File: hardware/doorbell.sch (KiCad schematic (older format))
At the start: 16 parts, among them J1 CONN_01X02, J2 CONN_01X09, J3 CONN_01X07, P1 DOOR, P2 STRIP_CONN, Q1 MMBT3904, U1 LD1117S33CTR, U2 4N25, U3 ESP-12

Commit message: Fix some library issues
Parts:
- removed P1: DOOR, Terminal_Blocks:TerminalBlock_Pheonix_MPT-2.54mm_3pol, symbol DOOR
- added P1: DOOR_CONN, Terminal_Blocks:TerminalBlock_Pheonix_MPT-2.54mm_3pol, symbol DOOR_CONN
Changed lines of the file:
@@
 EESchema Schematic File Version 2
-LIBS:borniers
 LIBS:power
 LIBS:device
@@
 Text GLabel 2100 1150 0    60   Input ~ 0
 VIN
-$Comp
-L DOOR P1
-U 1 1 573DA8E3
-P 1200 2050
-F 0 "P1" H 1100 2300 50  0000 C CNN
-F 1 "DOOR" H 1200 2240 40  0000 C CNN
-F 2 "Terminal_Blocks:TerminalBlock_Pheonix_MPT-2.54mm_3pol" H 1200 2050 60  0001 C CNN
-F 3 "" H 1200 2050 60  0000 C CNN
-	1    1200 2050
-	-1   0    0    1
-$EndComp
 Text GLabel 1550 2150 2    60   Input ~ 0
 VIN
@@
 	-1   0    0    1
 $EndComp
+$Comp
+L DOOR_CONN P1
+U 1 1 5744979E
+P 1350 2050
+F 0 "P1" H 1350 2250 50  0000 C CNN
+F 1 "DOOR_CONN" V 1450 2050 50  0000 C CNN
+F 2 "Terminal_Blocks:TerminalBlock_Pheonix_MPT-2.54mm_3pol" H 1350 2050 50  0001 C CNN
+F 3 "" H 1350 2050 50  0000 C CNN
+	1    1350 2050
+	-1   0    0    1
+$EndComp

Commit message: Shrink board, expand copper, change Q1 bom
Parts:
- removed Q1: MMBT3904, TO_SOT_Packages_SMD:SOT-23, symbol MMBT3904
- added Q1: BC_846B, TO_SOT_Packages_SMD:SOT-23_Handsoldering, symbol Q_NPN_BEC
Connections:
- net GND: now also Q1.2 (E)
- net at U2.2: now also Q1.3 (C)
- net at R6.2: now also Q1.1 (B)
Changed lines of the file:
@@
-$EndComp
-$Comp
-L MMBT3904 Q1
-U 1 1 574330E7
-P 4350 4650
-F 0 "Q1" H 4550 4725 50  0000 L CNN
-F 1 "MMBT3904" H 4550 4650 50  0000 L CNN
-F 2 "TO_SOT_Packages_SMD:SOT-23" H 4550 4575 50  0000 L CIN
-F 3 "" H 4350 4650 50  0000 L CNN
-	1    4350 4650
-	-1   0    0    1
 $EndComp
 $Comp
@@
 	-1   0    0    1
 $EndComp
+$Comp
+L Q_NPN_BEC Q1
+U 1 1 5745933D
+P 4350 4650
+F 0 "Q1" H 4650 4700 50  0000 R CNN
+F 1 "BC_846B" H 4950 4600 50  0000 R CNN
+F 2 "TO_SOT_Packages_SMD:SOT-23_Handsoldering" H 4550 4750 50  0001 C CNN
+F 3 "" H 4350 4650 50  0000 C CNN
+	1    4350 4650
+	-1   0    0    1
+$EndComp

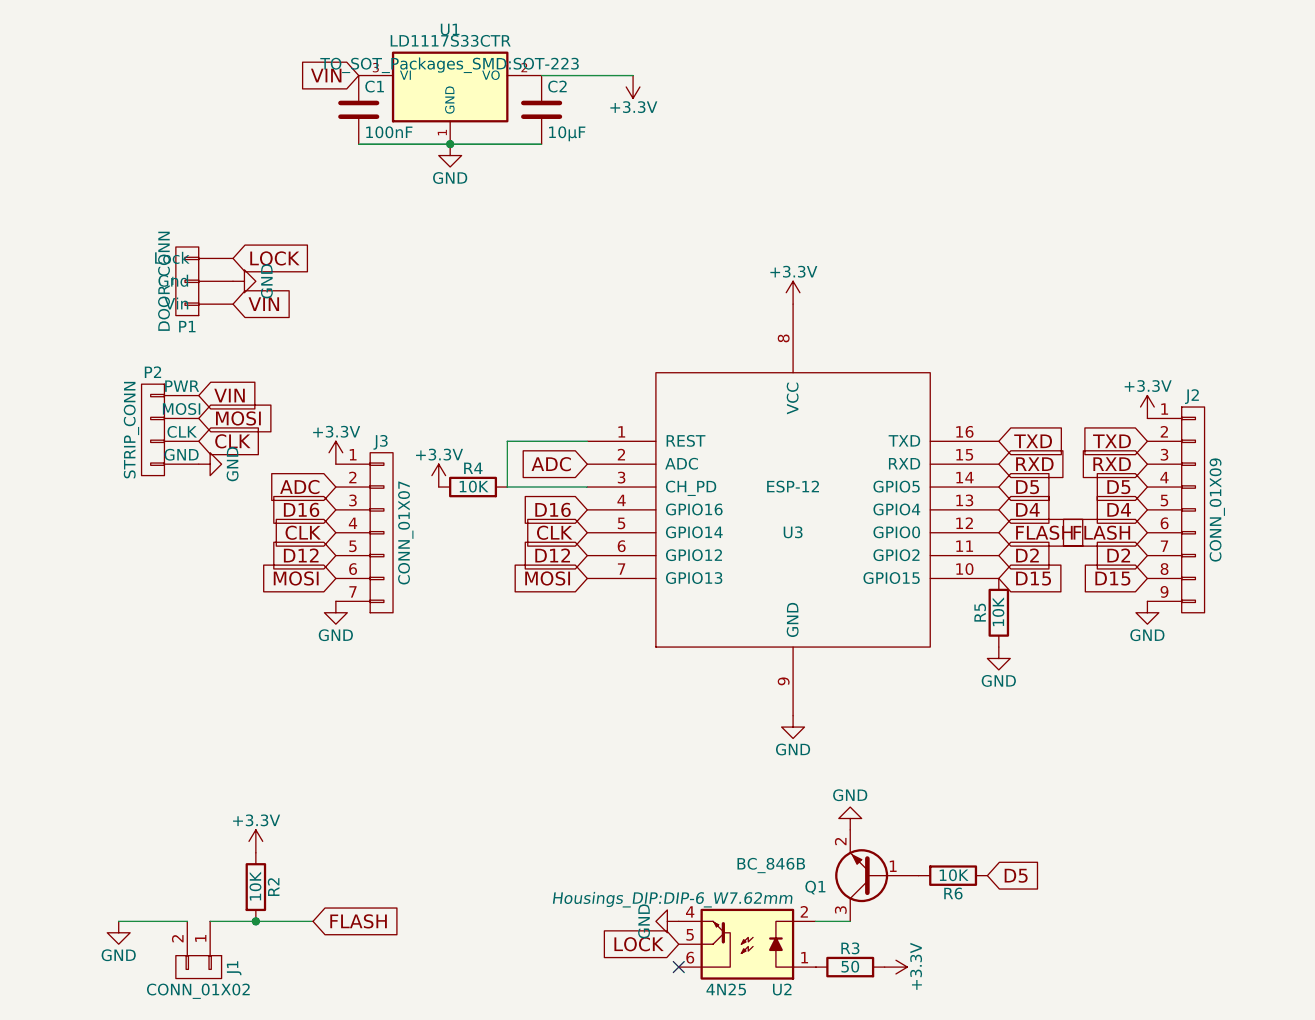
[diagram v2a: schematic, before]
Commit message: Convert to include a switching voltage regulator breakout
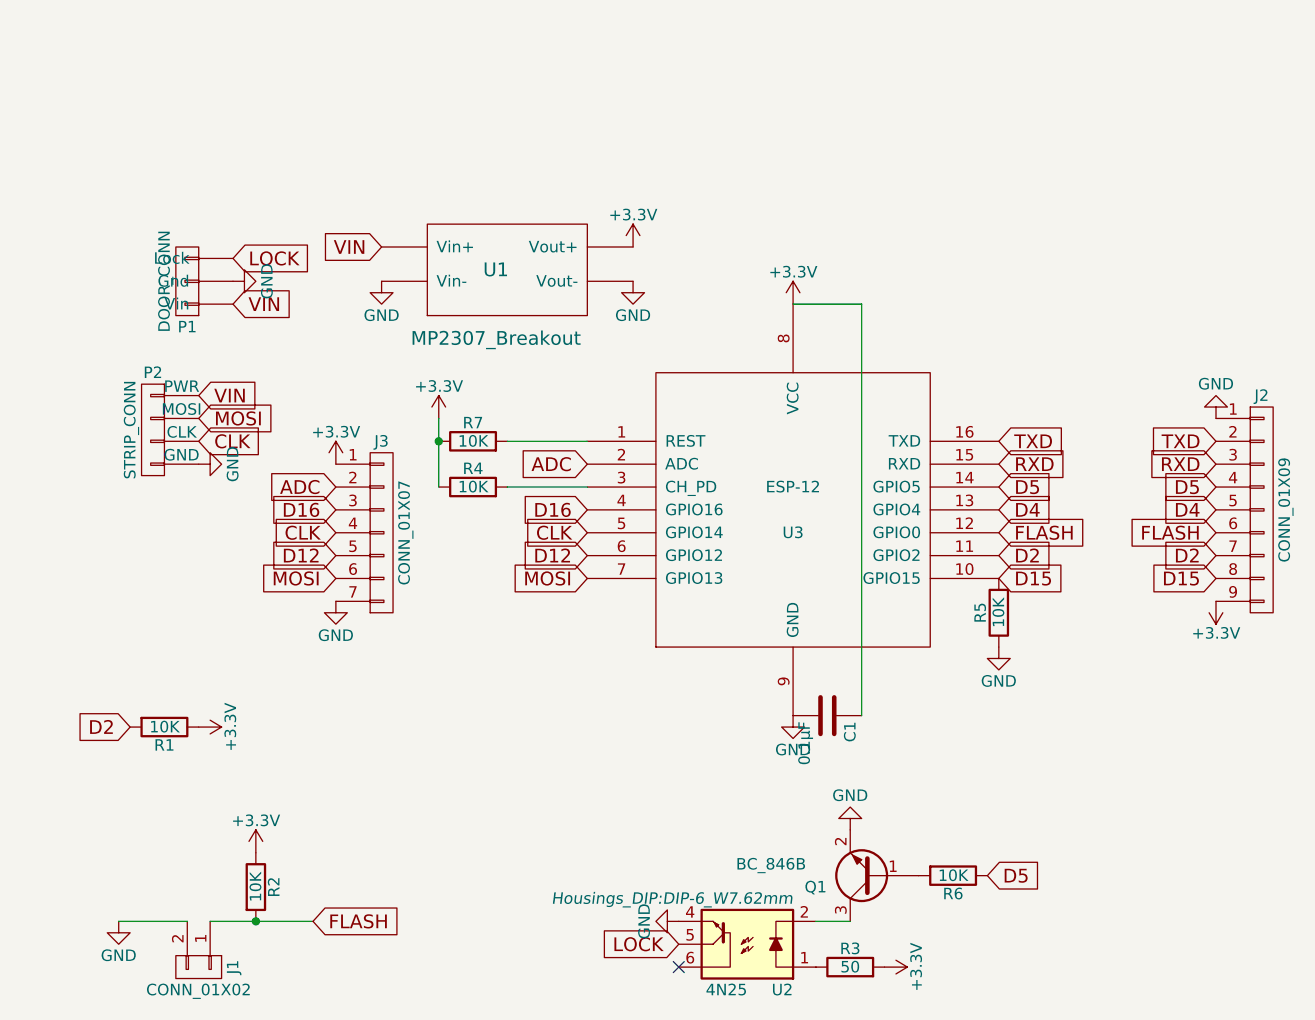
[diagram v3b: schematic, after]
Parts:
- removed C2: 10µF, Capacitors_SMD:C_0805_HandSoldering, symbol C
- removed U1: LD1117S33CTR, TO_SOT_Packages_SMD:SOT-223, symbol LD1117S33CTR
- added R1, R7: 10K, symbol R
- added U1: MP2307_Breakout, Doorbell:MP2307_Breakout, symbol MP2307_Breakout
- C1: value 100nF -> 0.1µF; footprint Capacitors_SMD:C_0805_HandSoldering -> Capacitors_SMD:C_1206_HandSoldering
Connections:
- net +3V3: now also C1.1, J2.9 (P9), R1.1, R7.1, U1.3 (Vout+); no longer J2.1 (P1)
- net D2: now also R1.2
- net GND: now also J2.1 (P1), U1.2 (Vin-), U1.4 (Vout-); no longer J2.9 (P9)
- net VIN: now also U1.1 (Vin+); no longer C1.1
- net at R4.2, U3.3 (CH_PD): no longer U3.1 (REST)
- new net: R7.2, U3.1 (REST)
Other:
- moved on the sheet: J2

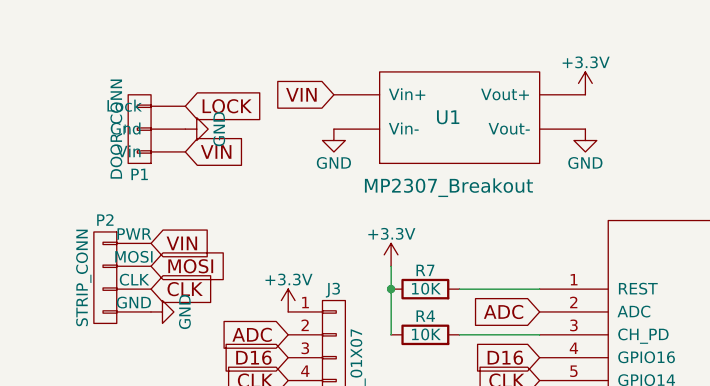
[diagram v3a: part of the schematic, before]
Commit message: Add Vin decoupling cap
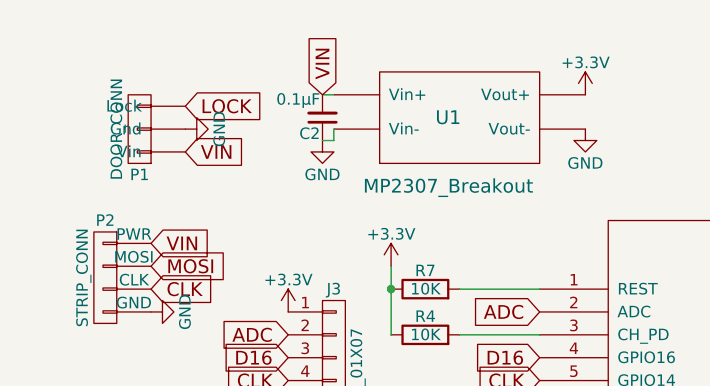
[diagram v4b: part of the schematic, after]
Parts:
- added C2: 0.1µF, Capacitors_SMD:C_1206_HandSoldering, symbol C_Small
- R1, R7: footprint (none) -> Resistors_ThroughHole:Resistor_Vertical_RM5mm
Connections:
- net GND: now also C2.1
- net VIN: now also C2.2
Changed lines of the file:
@@
 MOSI
 $Comp
-L GND #PWR14
+L GND #PWR01
 U 1 1 573B5931
 P 4000 3950
-F 0 "#PWR14" H 4000 3700 50  0001 C CNN
+F 0 "#PWR01" H 4000 3700 50  0001 C CNN
 F 1 "GND" H 4000 3800 50  0000 C CNN
 F 2 "" H 4000 3950 50  0000 C CNN
@@
 $EndComp
 $Comp
-L +3.3V #PWR13
+L +3.3V #PWR02
 U 1 1 573B599B
 P 4000 2150
-F 0 "#PWR13" H 4000 2000 50  0001 C CNN
+F 0 "#PWR02" H 4000 2000 50  0001 C CNN
 F 1 "+3.3V" H 4000 2290 50  0000 C CNN
 F 2 "" H 4000 2150 50  0000 C CNN
@@
 $EndComp
 $Comp
-L GND #PWR17
+L GND #PWR03
 U 1 1 573C748A
 P 4900 3650
-F 0 "#PWR17" H 4900 3400 50  0001 C CNN
+F 0 "#PWR03" H 4900 3400 50  0001 C CNN
 F 1 "GND" H 4900 3500 50  0000 C CNN
 F 2 "" H 4900 3650 50  0000 C CNN
@@
 	3100 2950 2750 2950
 $Comp
-L +3.3V #PWR9
+L +3.3V #PWR04
 U 1 1 573C76A9
 P 2450 2650
-F 0 "#PWR9" H 2450 2500 50  0001 C CNN
+F 0 "#PWR04" H 2450 2500 50  0001 C CNN
 F 1 "+3.3V" H 2450 2790 50  0000 C CNN
 F 2 "" H 2450 2650 50  0000 C CNN
@@
 $EndComp
 $Comp
-L GND #PWR1
+L GND #PWR05
 U 1 1 573C7B17
 P 1050 4850
-F 0 "#PWR1" H 1050 4600 50  0001 C CNN
+F 0 "#PWR05" H 1050 4600 50  0001 C CNN
 F 1 "GND" H 1050 4700 50  0000 C CNN
 F 2 "" H 1050 4850 50  0000 C CNN
@@
 $EndComp
 $Comp
-L +3.3V #PWR5
+L +3.3V #PWR06
 U 1 1 573C7B23
 P 1650 4550
-F 0 "#PWR5" H 1650 4400 50  0001 C CNN
+F 0 "#PWR06" H 1650 4400 50  0001 C CNN
 F 1 "+3.3V" H 1650 4690 50  0000 C CNN
 F 2 "" H 1650 4550 50  0000 C CNN
@@
 LOCK
 $Comp
-L GND #PWR12
+L GND #PWR07
 U 1 1 573C8ED6
 P 3500 4850
-F 0 "#PWR12" H 3500 4600 50  0001 C CNN
+F 0 "#PWR07" H 3500 4600 50  0001 C CNN
 F 1 "GND" H 3500 4700 50  0000 C CNN
 F 2 "" H 3500 4850 50  0000 C CNN
@@
 $EndComp
 $Comp
-L +3.3V #PWR16
+L +3.3V #PWR08
 U 1 1 573C96C2
 P 4400 5050
-F 0 "#PWR16" H 4400 4900 50  0001 C CNN
+F 0 "#PWR08" H 4400 4900 50  0001 C CNN
 F 1 "+3.3V" H 4400 5190 50  0000 C CNN
 F 2 "" H 4400 5050 50  0000 C CNN
@@
 	4100 4850 4250 4850
 $Comp
-L GND #PWR15
+L GND #PWR09
 U 1 1 573C9852
 P 4250 4450
-F 0 "#PWR15" H 4250 4200 50  0001 C CNN
+F 0 "#PWR09" H 4250 4200 50  0001 C CNN
 F 1 "GND" H 4250 4300 50  0000 C CNN
 F 2 "" H 4250 4450 50  0000 C CNN
@@
 LOCK
 $Comp
-L GND #PWR4
+L GND #PWR010
 U 1 1 573DAD82
 P 1550 2050
-F 0 "#PWR4" H 1550 1800 50  0001 C CNN
+F 0 "#PWR010" H 1550 1800 50  0001 C CNN
 F 1 "GND" H 1550 1900 50  0000 C CNN
 F 2 "" H 1550 2050 50  0000 C CNN
@@
 CLK
 $Comp
-L GND #PWR2
+L GND #PWR011
 U 1 1 573DA44F
 P 1400 2850
-F 0 "#PWR2" H 1400 2600 50  0001 C CNN
+F 0 "#PWR011" H 1400 2600 50  0001 C CNN
 F 1 "GND" H 1400 2700 50  0000 C CNN
 F 2 "" H 1400 2850 50  0000 C CNN
@@
 $EndComp
 $Comp
-L +3.3V #PWR19
+L +3.3V #PWR012
 U 1 1 57430C52
 P 5850 3450
-F 0 "#PWR19" H 5850 3300 50  0001 C CNN
+F 0 "#PWR012" H 5850 3300 50  0001 C CNN
 F 1 "+3.3V" H 5850 3590 50  0000 C CNN
 F 2 "" H 5850 3450 50  0000 C CNN
@@
 D15
 $Comp
-L GND #PWR18
+L GND #PWR013
 U 1 1 57430E1D
 P 5850 2650
-F 0 "#PWR18" H 5850 2400 50  0001 C CNN
+F 0 "#PWR013" H 5850 2400 50  0001 C CNN
 F 1 "GND" H 5850 2500 50  0000 C CNN
 F 2 "" H 5850 2650 50  0000 C CNN
@@
 $EndComp
 $Comp
-L +3.3V #PWR6
+L +3.3V #PWR014
 U 1 1 57431209
 P 2000 2850
-F 0 "#PWR6" H 2000 2700 50  0001 C CNN
+F 0 "#PWR014" H 2000 2700 50  0001 C CNN
 F 1 "+3.3V" H 2000 2990 50  0000 C CNN
 F 2 "" H 2000 2850 50  0000 C CNN
@@
 $EndComp
 $Comp
-L GND #PWR7
+L GND #PWR015
 U 1 1 5743123D
 P 2000 3450
-F 0 "#PWR7" H 2000 3200 50  0001 C CNN
+F 0 "#PWR015" H 2000 3200 50  0001 C CNN
 F 1 "GND" H 2000 3300 50  0000 C CNN
 F 2 "" H 2000 3450 50  0000 C CNN
@@
 	1    0    0    -1
 $EndComp
-Text GLabel 2200 1900 0    60   Input ~ 0
+Text GLabel 2150 1900 1    60   Input ~ 0
 VIN
 $Comp
-L GND #PWR8
+L GND #PWR016
 U 1 1 574C1920
-P 2200 2050
-F 0 "#PWR8" H 2200 1800 50  0001 C CNN
-F 1 "GND" H 2200 1900 50  0000 C CNN
-F 2 "" H 2200 2050 50  0000 C CNN
-F 3 "" H 2200 2050 50  0000 C CNN
-	1    2200 2050
-	1    0    0    -1
-$EndComp
-$Comp
-L GND #PWR11
+P 2150 2100
+F 0 "#PWR016" H 2150 1850 50  0001 C CNN
+F 1 "GND" H 2150 1950 50  0000 C CNN
+F 2 "" H 2150 2100 50  0000 C CNN
+F 3 "" H 2150 2100 50  0000 C CNN
+	1    2150 2100
+	1    0    0    -1
+$EndComp
+$Comp
+L GND #PWR017
 U 1 1 574C19BB
 P 3300 2050
-F 0 "#PWR11" H 3300 1800 50  0001 C CNN
+F 0 "#PWR017" H 3300 1800 50  0001 C CNN
 F 1 "GND" H 3300 1900 50  0000 C CNN
 F 2 "" H 3300 2050 50  0000 C CNN
@@
 $EndComp
 $Comp
-L +3.3V #PWR10
+L +3.3V #PWR018
 U 1 1 574C19ED
 P 3300 1900
-F 0 "#PWR10" H 3300 1750 50  0001 C CNN
+F 0 "#PWR018" H 3300 1750 50  0001 C CNN
 F 1 "+3.3V" H 3300 2040 50  0000 C CNN
 F 2 "" H 3300 1900 50  0000 C CNN
@@
 F 0 "R7" V 2680 2750 50  0000 C CNN
 F 1 "10K" V 2600 2750 50  0000 C CNN
-F 2 "" V 2530 2750 50  0000 C CNN
+F 2 "Resistors_ThroughHole:Resistor_Vertical_RM5mm" V 2530 2750 50  0001 C CNN
 F 3 "" H 2600 2750 50  0000 C CNN
 	1    2600 2750
@@
 F 0 "R1" V 1330 4000 50  0000 C CNN
 F 1 "10K" V 1250 4000 50  0000 C CNN
-F 2 "" V 1180 4000 50  0000 C CNN
+F 2 "Resistors_ThroughHole:Resistor_Vertical_RM5mm" V 1180 4000 50  0001 C CNN
 F 3 "" H 1250 4000 50  0000 C CNN
 	1    1250 4000
@@
 $EndComp
 $Comp
-L +3.3V #PWR3
+L +3.3V #PWR019
 U 1 1 574C2CE0
 P 1400 4000
-F 0 "#PWR3" H 1400 3850 50  0001 C CNN
+F 0 "#PWR019" H 1400 3850 50  0001 C CNN
 F 1 "+3.3V" H 1400 4140 50  0000 C CNN
 F 2 "" H 1400 4000 50  0000 C CNN
@@
 	0    1    1    0
 $EndComp
+$Comp
+L C_Small C2
+U 1 1 574C3EED
+P 2150 2000
+F 0 "C2" H 2160 2070 50  0000 L CNN
+F 1 "0.1µF" H 2160 1920 50  0000 L CNN
+F 2 "Capacitors_SMD:C_1206_HandSoldering" H 2150 2000 50  0001 C CNN
+F 3 "" H 2150 2000 50  0000 C CNN
+	1    2150 2000
+	-1   0    0    1
+$EndComp
+Wire Wire Line
+	2200 1900 2150 1900
+Wire Wire Line
+	2200 2050 2200 2100
+Wire Wire Line
+	2200 2100 2150 2100
 $EndSCHEMATC
